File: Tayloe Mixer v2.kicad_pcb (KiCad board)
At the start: 2 copper layers, 118.8 x 62 mm, 38 parts, among them J1 BNC, J2 Pad, J3 Audio_Jack, J4 Conn_01x04_Female, J5 Pad, T1 6:31, T2 31:6, T3 T50_SPLITTER, U1 LM7805_TO220, U2 FST3253, U3 LM358, U4 si5351, U5 LD33V

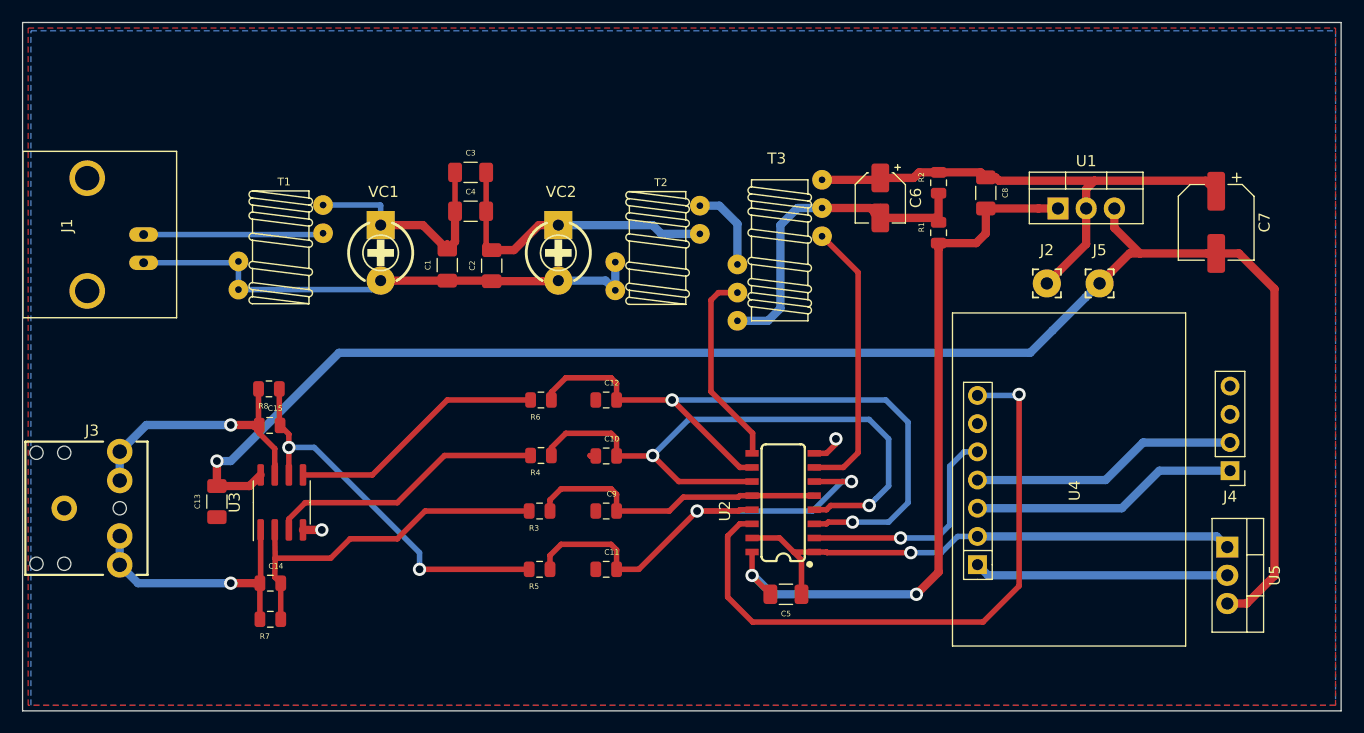
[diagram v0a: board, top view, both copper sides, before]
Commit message: swapping caps
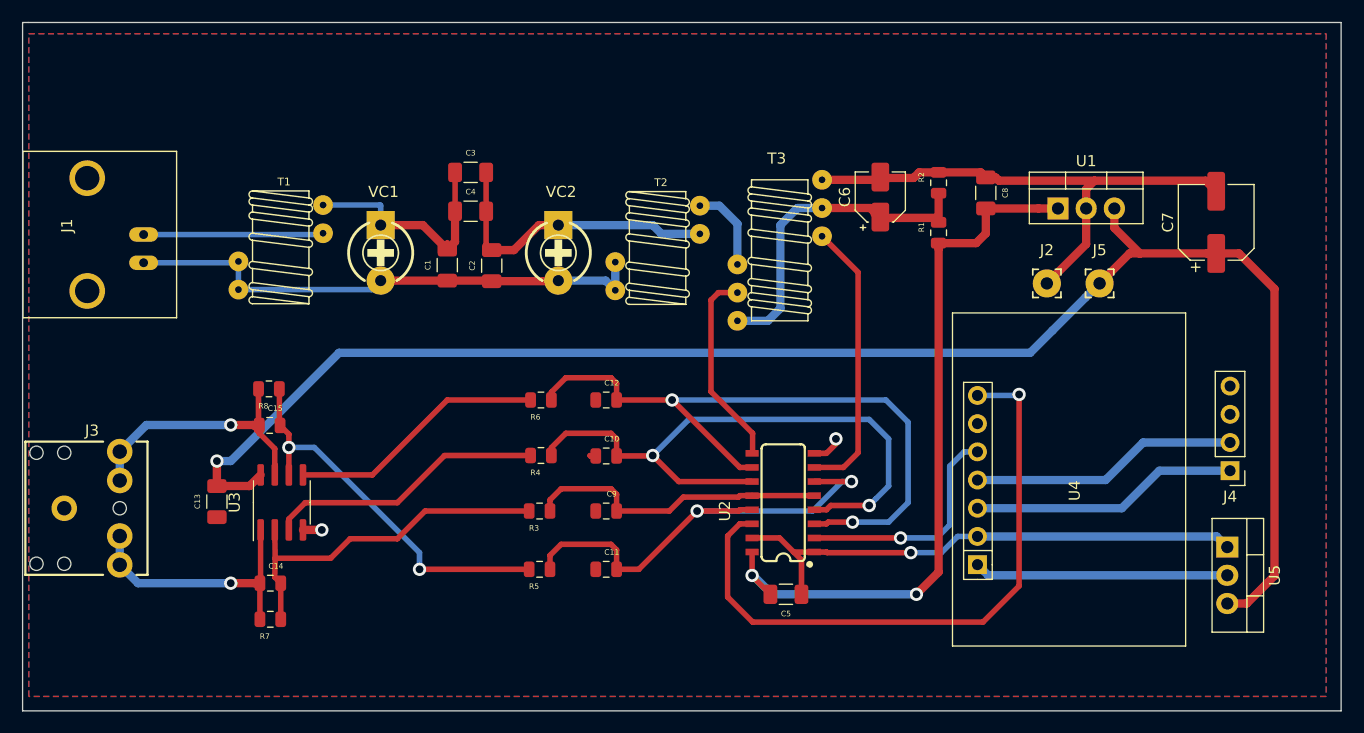
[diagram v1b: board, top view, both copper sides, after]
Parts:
- moved C6 0.08 mm to (175.8, 63.0), turned to 90 degrees
- turned C7 to 90 degrees
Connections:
- C6 pad 1: GND -> Net-(C6-Pad1)
- C6 pad 2: Net-(C6-Pad2) -> GND
- C7 pad 1: GND -> +12V
- C7 pad 2: +12V -> GND
- J4 pad 3: (no net) -> Net-(J4-Pad3)
- R1 pad 2: Net-(C6-Pad2) -> Net-(C6-Pad1)
- R2 pad 1: Net-(C6-Pad2) -> Net-(C6-Pad1)
- T3 pad C2A: Net-(C6-Pad2) -> Net-(C6-Pad1)
- T3 pad C3B: Net-(C6-Pad2) -> Net-(C6-Pad1)
- U4 pad 1: (no net) -> Net-(U4-Pad1)
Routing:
- net Net-(C6-Pad2): track 30.6 -> 0.00 mm
- net Net-(C6-Pad1): track 0.00 -> 30.6 mm

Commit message: gg
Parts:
- renumbered C1 to C2, C5 to C25, C2 to C5, VC2 to VC6
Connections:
- J4 pad 3: Net-(J4-Pad3) -> (no net)
- U4 pad 1: Net-(U4-Pad1) -> (no net)
